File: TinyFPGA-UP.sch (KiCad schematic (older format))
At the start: 35 parts, among them J1 Conn_01x14, J2 Conn_01x14, J3 USB_B_Micro, J4 Conn_02x08_Odd_Even, J5 Conn_02x03_Odd_Even, SW1 SW_Push, U1 iCE40-UP5K-SG48, U2 MIC5504-3.3, U3 DSC6001CI2A, U4 MIC5365-1.2, U5 AT25SF081

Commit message: Update routing
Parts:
- added C10, C11, C12, C22: 10nF, Capacitor_SMD:C_0402_1005Metric, symbol Device:C_Small
- added C13, C19, C20, C21: 1uF, Capacitor_SMD:C_0402_1005Metric, symbol Device:C_Small
- added C14, C15, C16, C18, C7, C9: 100nF, Capacitor_SMD:C_0402_1005Metric, symbol Device:C_Small
- added C6: 10uF, Capacitor_SMD:C_0402_1005Metric, symbol Device:C_Small
- added D4: RGB, DRA818:LTST-C19HE1WT, symbol Device:LED_BGRA
- added R11, R16, R17: 0, Resistor_SMD:R_0402_1005Metric, symbol Device:R_Small
- added R12, R13, R14: 100, Resistor_SMD:R_0402_1005Metric, symbol Device:R_Small
- added R15: DNP, Resistor_SMD:R_0402_1005Metric, symbol Device:R_Small
- J4: value Conn_02x08_Odd_Even -> Conn_02x08
- J5: value Conn_02x03_Odd_Even -> Conn_02x03
- R8: value 270 -> 2.2k
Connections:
- net +1V2: now also C10.1, C14.1, C19.1, C6.1, C9.1
- net +3V3: now also R8.1, C11.1, C12.1, C13.1, C15.1, C16.1, C18.1, C20.1, C21.1, C22.1, C7.1, D4.4 (A); no longer D1.2 (A)
- net 29B: now also J4.7 (Pin_7), R16.1
- net 31B: now also J4.8 (Pin_8), R17.1
- net CDONE: now also R11.2
- net GND: now also D1.1 (K), D2.1 (K), C10.2, C11.2, C12.2, C13.2, C14.2, C15.2, C16.2, C18.2, C19.2, C20.2, C21.2, C22.2, C6.2, C7.2, C9.2, R15.2; no longer R8.2, R9.2
- net HOLD: now also R16.2
- net LED: now also R9.1; no longer D2.2 (A)
- net RGB0: now also J4.1 (Pin_1), R12.1
- net RGB1: now also J4.5 (Pin_5), R13.1
- net RGB2: now also J4.2 (Pin_2), R14.1
- net WP: now also R15.1, R17.2
- new net: D1.2 (A), R11.1, R8.2
- new net: D4.1 (BK), R14.2
- new net: D4.2 (GK), R13.2
- new net: D4.3 (RK), R12.2
- new net: D2.2 (A), R9.2
- no-connect marks 1 -> 2
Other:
- note added: "Optional"
- moved on the sheet: C1, C17, C2, C3, C4, C8, D1, D2, D3, J1, J2, J3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

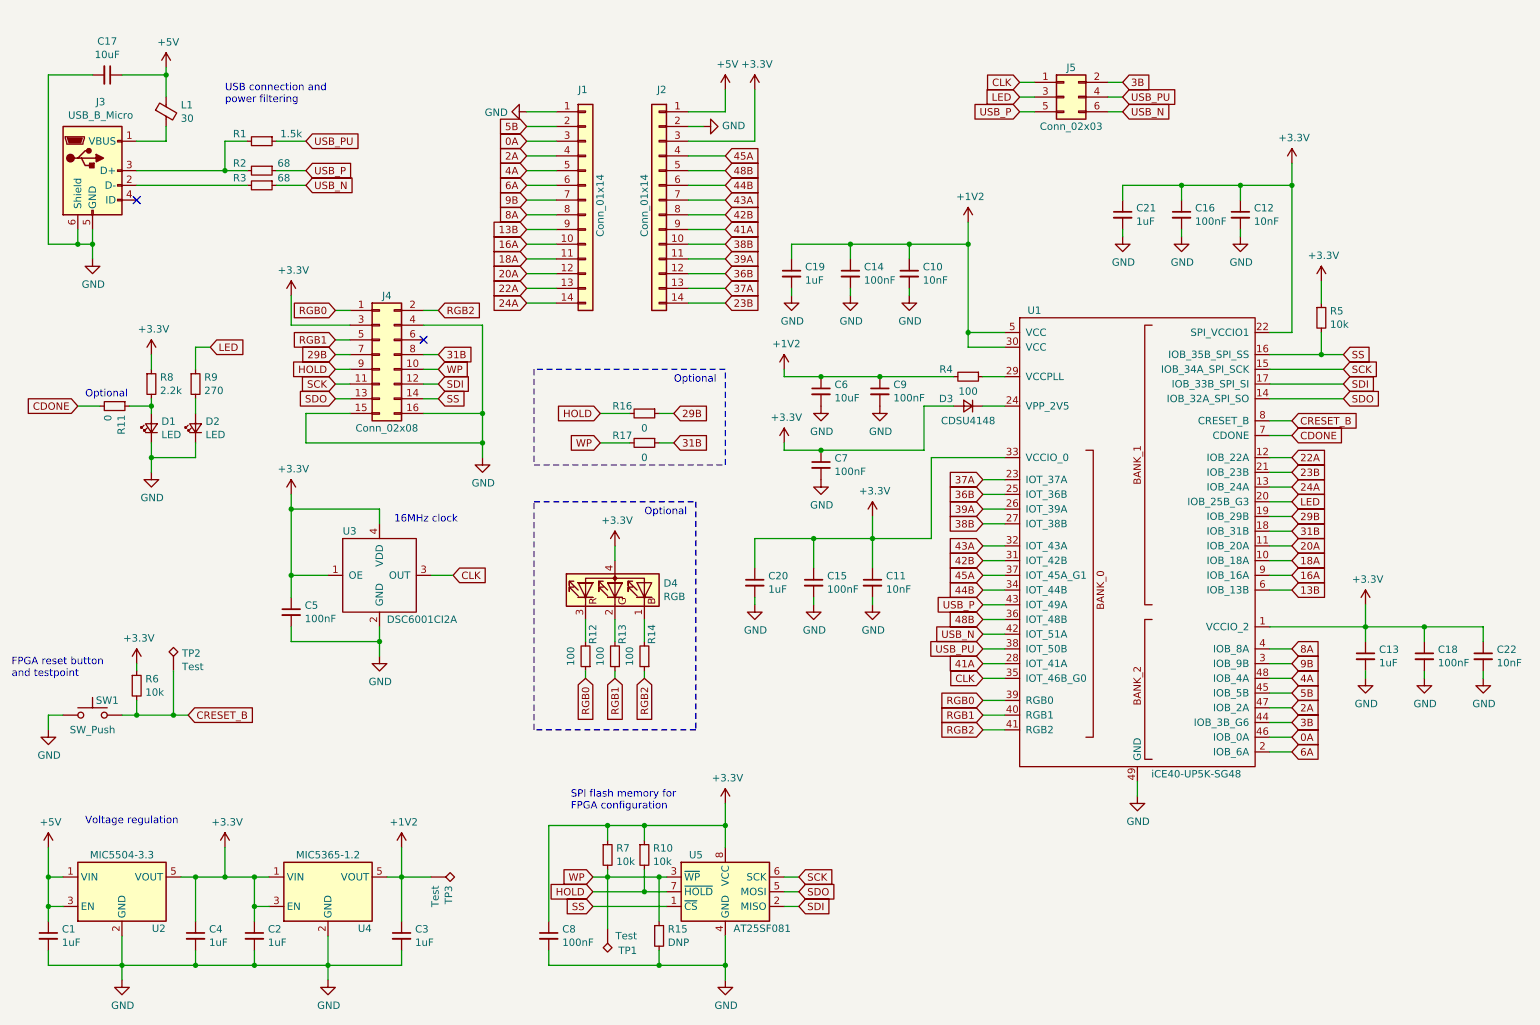
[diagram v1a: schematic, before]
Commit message: Make LED, WP, HLC compatible
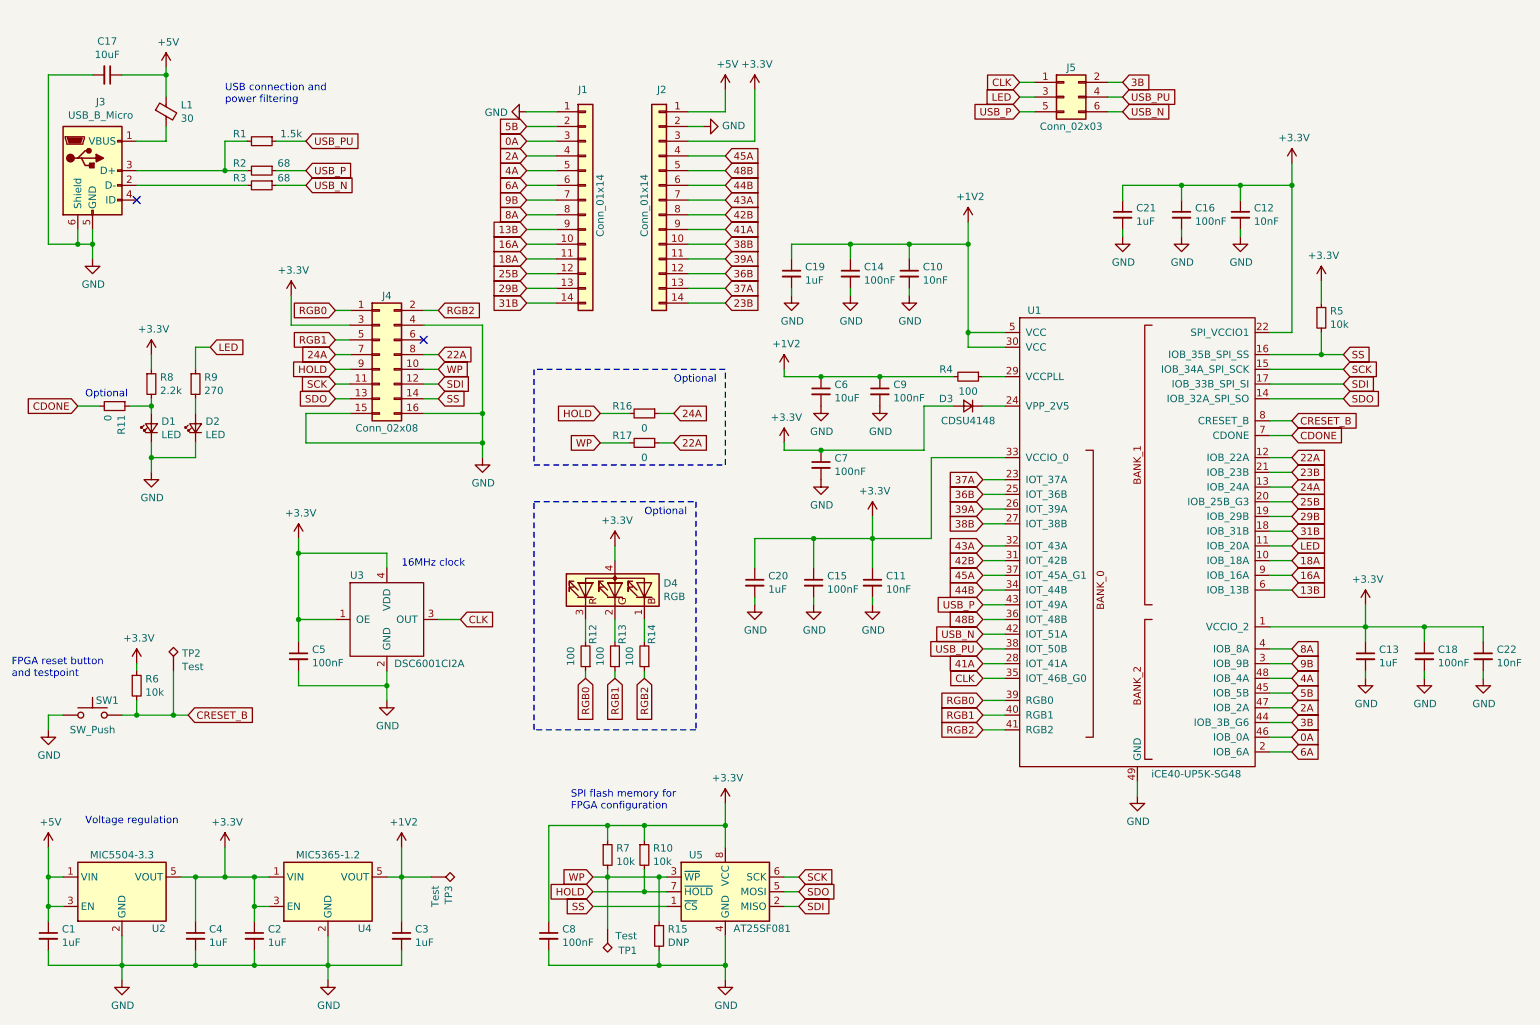
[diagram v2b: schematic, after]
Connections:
- net 22A: now also J4.8 (Pin_8), R17.1; no longer J1.13 (Pin_13)
- net 24A: now also J4.7 (Pin_7), R16.1; no longer J1.14 (Pin_14)
- net 29B: now also J1.13 (Pin_13); no longer J4.7 (Pin_7), R16.1
- net 31B: now also J1.14 (Pin_14); no longer J4.8 (Pin_8), R17.1
- net LED: now also U1.11 (IOB_20A); no longer U1.20 (IOB_25B_G3)
- net 20A renamed 25B
- net 25B: now also U1.20 (IOB_25B_G3); no longer U1.11 (IOB_20A)
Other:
- moved on the sheet: C5, U3
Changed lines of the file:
@@
 Text GLabel 7350 4650 0    50   Input ~ 0
 USB_P
-Text GLabel 9450 3950 2    50   Input ~ 0
+Text GLabel 9450 4250 2    50   Input ~ 0
 LED
 Text GLabel 7350 5150 0    50   Input ~ 0
@@
 Text GLabel 9450 4350 2    50   Input ~ 0
 18A
-Text GLabel 9450 4250 2    50   Input ~ 0
-20A
+Text GLabel 9450 3950 2    50   Input ~ 0
+25B
 Text GLabel 9450 3650 2    50   Input ~ 0
 22A
@@
 18A
 Text GLabel 4250 2400 0    50   Input ~ 0
-20A
-Text GLabel 4250 2500 0    50   Input ~ 0
+25B
+Text GLabel 3650 2950 2    50   Input ~ 0
 22A
 Wire Wire Line
@@
 Wire Wire Line
 	9300 3750 9450 3750
+Text GLabel 2950 2950 0    50   Input ~ 0
+24A
 Text GLabel 4250 2600 0    50   Input ~ 0
-24A
-Text GLabel 3650 2950 2    50   Input ~ 0
 31B
-Text GLabel 2950 2950 0    50   Input ~ 0
+Text GLabel 4250 2500 0    50   Input ~ 0
 29B
 Text GLabel 5600 2600 2    50   Input ~ 0
@@
 L DRA818:DSC6001CI2A U3
 U 1 1 5C0F5A23
-P 3250 4450
-F 0 "U3" H 3000 4750 50  0000 L CNN
-F 1 "DSC6001CI2A" H 3300 4150 50  0000 L CNN
-F 2 "Crystal:Crystal_SMD_3225-4Pin_3.2x2.5mm" H 3250 4450 50  0001 C CNN
-F 3 "" H 3250 4450 50  0001 C CNN
-	1    3250 4450
+P 3300 4750
+F 0 "U3" H 3050 5050 50  0000 L CNN
+F 1 "DSC6001CI2A" H 3350 4450 50  0000 L CNN
+F 2 "Crystal:Crystal_SMD_3225-4Pin_3.2x2.5mm" H 3300 4750 50  0001 C CNN
+F 3 "" H 3300 4750 50  0001 C CNN
+	1    3300 4750
 	1    0    0    -1
 $EndComp
@@
 L Device:C_Small C5
 U 1 1 5C0F5CED
-P 2650 4700
-F 0 "C5" H 2742 4746 50  0000 L CNN
-F 1 "100nF" H 2742 4655 50  0000 L CNN
-F 2 "Capacitor_SMD:C_0402_1005Metric" H 2650 4700 50  0001 C CNN
-F 3 "~" H 2650 4700 50  0001 C CNN
-	1    2650 4700
+P 2700 5000
+F 0 "C5" H 2792 5046 50  0000 L CNN
+F 1 "100nF" H 2792 4955 50  0000 L CNN
+F 2 "Capacitor_SMD:C_0402_1005Metric" H 2700 5000 50  0001 C CNN
+F 3 "~" H 2700 5000 50  0001 C CNN
+	1    2700 5000
 	1    0    0    -1
 $EndComp
@@
 L power:GND #PWR0120
 U 1 1 5C0F5D58
-P 3250 5000
-F 0 "#PWR0120" H 3250 4750 50  0001 C CNN
-F 1 "GND" H 3255 4827 50  0000 C CNN
-F 2 "" H 3250 5000 50  0001 C CNN
-F 3 "" H 3250 5000 50  0001 C CNN
-	1    3250 5000
-	1    0    0    -1
-$EndComp
-Wire Wire Line
-	3250 4800 3250 4900
-Wire Wire Line
-	3250 4900 2650 4900
-Wire Wire Line
-	2650 4900 2650 4800
-Connection ~ 3250 4900
-Wire Wire Line
-	3250 4900 3250 5000
-Wire Wire Line
-	2900 4450 2650 4450
-Wire Wire Line
-	2650 4450 2650 4600
-Wire Wire Line
-	3250 4100 3250 4000
-Wire Wire Line
-	3250 4000 2650 4000
-Wire Wire Line
-	2650 4000 2650 4450
-Connection ~ 2650 4450
-Wire Wire Line
-	3600 4450 3750 4450
+P 3300 5300
+F 0 "#PWR0120" H 3300 5050 50  0001 C CNN
+F 1 "GND" H 3305 5127 50  0000 C CNN
+F 2 "" H 3300 5300 50  0001 C CNN
+F 3 "" H 3300 5300 50  0001 C CNN
+	1    3300 5300
+	1    0    0    -1
+$EndComp
+Wire Wire Line
+	3300 5100 3300 5200
+Wire Wire Line
+	3300 5200 2700 5200
+Wire Wire Line
+	2700 5200 2700 5100
+Connection ~ 3300 5200
+Wire Wire Line
+	3300 5200 3300 5300
+Wire Wire Line
+	2950 4750 2700 4750
+Wire Wire Line
+	2700 4750 2700 4900
+Wire Wire Line
+	3300 4400 3300 4300
+Wire Wire Line
+	3300 4300 2700 4300
+Wire Wire Line
+	2700 4300 2700 4750
+Connection ~ 2700 4750
+Wire Wire Line
+	3650 4750 3800 4750
 $Comp
 L power:+3.3V #PWR0121
 U 1 1 5C12A42C
-P 2650 3900
-F 0 "#PWR0121" H 2650 3750 50  0001 C CNN
-F 1 "+3.3V" H 2665 4073 50  0000 C CNN
-F 2 "" H 2650 3900 50  0001 C CNN
-F 3 "" H 2650 3900 50  0001 C CNN
-	1    2650 3900
-	1    0    0    -1
-$EndComp
-Wire Wire Line
-	2650 3900 2650 4000
-Connection ~ 2650 4000
-Text GLabel 3750 4450 2    50   Input ~ 0
+P 2700 4200
+F 0 "#PWR0121" H 2700 4050 50  0001 C CNN
+F 1 "+3.3V" H 2715 4373 50  0000 C CNN
+F 2 "" H 2700 4200 50  0001 C CNN
+F 3 "" H 2700 4200 50  0001 C CNN
+	1    2700 4200
+	1    0    0    -1
+$EndComp
+Wire Wire Line
+	2700 4200 2700 4300
+Connection ~ 2700 4300
+Text GLabel 3800 4750 2    50   Input ~ 0
 CLK
 Wire Wire Line
@@
 Text Notes 1250 6150 0    50   ~ 0
 Voltage regulation
-Text Notes 3350 4100 0    50   ~ 0
+Text Notes 3400 4400 0    50   ~ 0
 16MHz clock
 Wire Wire Line
@@
 Text GLabel 4750 3350 0    50   Input ~ 0
 HOLD
-Text GLabel 5250 3350 2    50   Input ~ 0
-29B
 Text GLabel 4750 3550 0    50   Input ~ 0
 WP
-Text GLabel 5250 3550 2    50   Input ~ 0
-31B
 Wire Wire Line
 	4750 3350 4950 3350
@@
 Wire Wire Line
 	9950 5150 9950 5100
+Text GLabel 5250 3550 2    50   Input ~ 0
+22A
+Text GLabel 5250 3350 2    50   Input ~ 0
+24A
 $EndSCHEMATC

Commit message: Minor changes
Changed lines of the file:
@@
 Text GLabel 5250 3350 2    50   Input ~ 0
 24A
+$Comp
+L power:PWR_FLAG #FLG?
+U 1 1 5BF04228
+P 2150 1000
+F 0 "#FLG?" H 2150 1075 50  0001 C CNN
+F 1 "PWR_FLAG" H 2150 1174 50  0000 C CNN
+F 2 "" H 2150 1000 50  0001 C CNN
+F 3 "~" H 2150 1000 50  0001 C CNN
+	1    2150 1000
+	1    0    0    -1
+$EndComp
+Wire Wire Line
+	1800 1050 2150 1050
+Wire Wire Line
+	2150 1050 2150 1000
 $EndSCHEMATC

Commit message: Add comments
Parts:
- R12, R13, R14: value 100 -> 1k
- R9: value 270 -> 1k
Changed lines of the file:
@@
 P 2000 3150
 F 0 "R9" H 2059 3196 50  0000 L CNN
-F 1 "270" H 2059 3105 50  0000 L CNN
+F 1 "1k" H 2059 3105 50  0000 L CNN
 F 2 "Resistor_SMD:R_0402_1005Metric" H 2000 3150 50  0001 C CNN
 F 3 "~" H 2000 3150 50  0001 C CNN
@@
 P 4650 5000
 F 0 "R12" V 4600 4850 50  0000 C CNN
-F 1 "100" V 4750 5000 50  0000 C CNN
+F 1 "1k" V 4750 5000 50  0000 C CNN
 F 2 "Resistor_SMD:R_0402_1005Metric" H 4650 5000 50  0001 C CNN
 F 3 "~" H 4650 5000 50  0001 C CNN
@@
 P 4850 5000
 F 0 "R13" V 4800 4850 50  0000 C CNN
-F 1 "100" V 4950 5000 50  0000 C CNN
+F 1 "1k" V 4950 5000 50  0000 C CNN
 F 2 "Resistor_SMD:R_0402_1005Metric" H 4850 5000 50  0001 C CNN
 F 3 "~" H 4850 5000 50  0001 C CNN
@@
 P 5050 5000
 F 0 "R14" V 5000 4850 50  0000 C CNN
-F 1 "100" V 5150 5000 50  0000 C CNN
+F 1 "1k" V 5150 5000 50  0000 C CNN
 F 2 "Resistor_SMD:R_0402_1005Metric" H 5050 5000 50  0001 C CNN
 F 3 "~" H 5050 5000 50  0001 C CNN
